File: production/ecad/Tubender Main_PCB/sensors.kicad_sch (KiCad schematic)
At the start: 6 parts, among them J10 640387-5, J14 640387-3, J5 640387-6, J6 640387-6, J8 640387-6, J9 640387-5

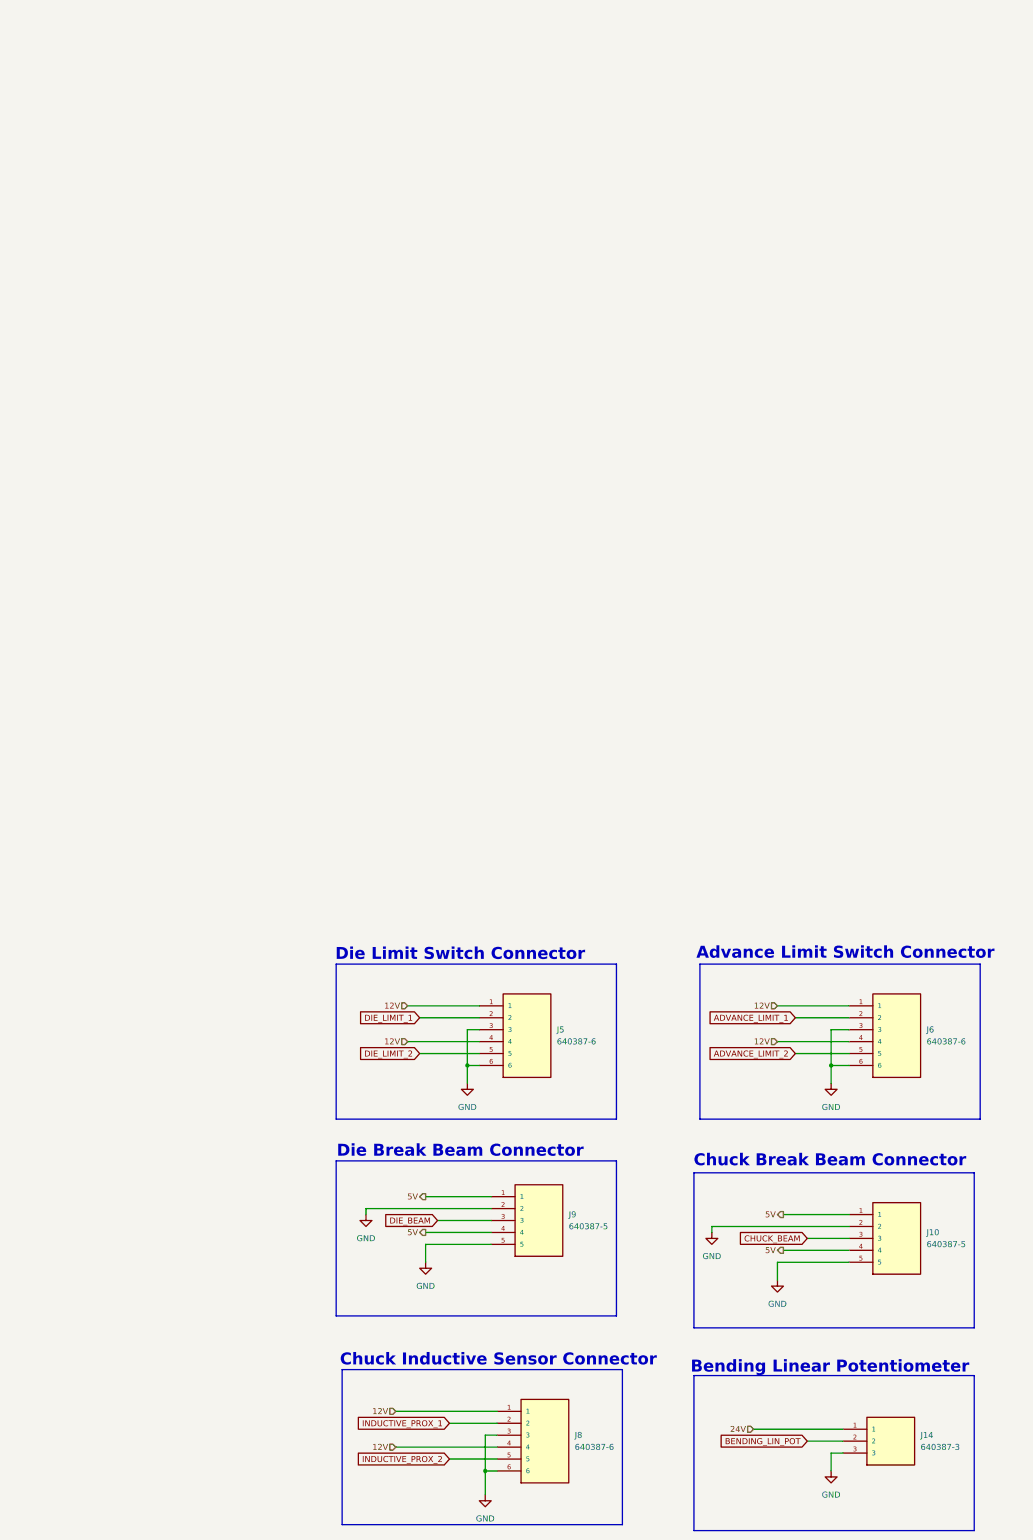
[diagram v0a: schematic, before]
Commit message: Fixed the Nets
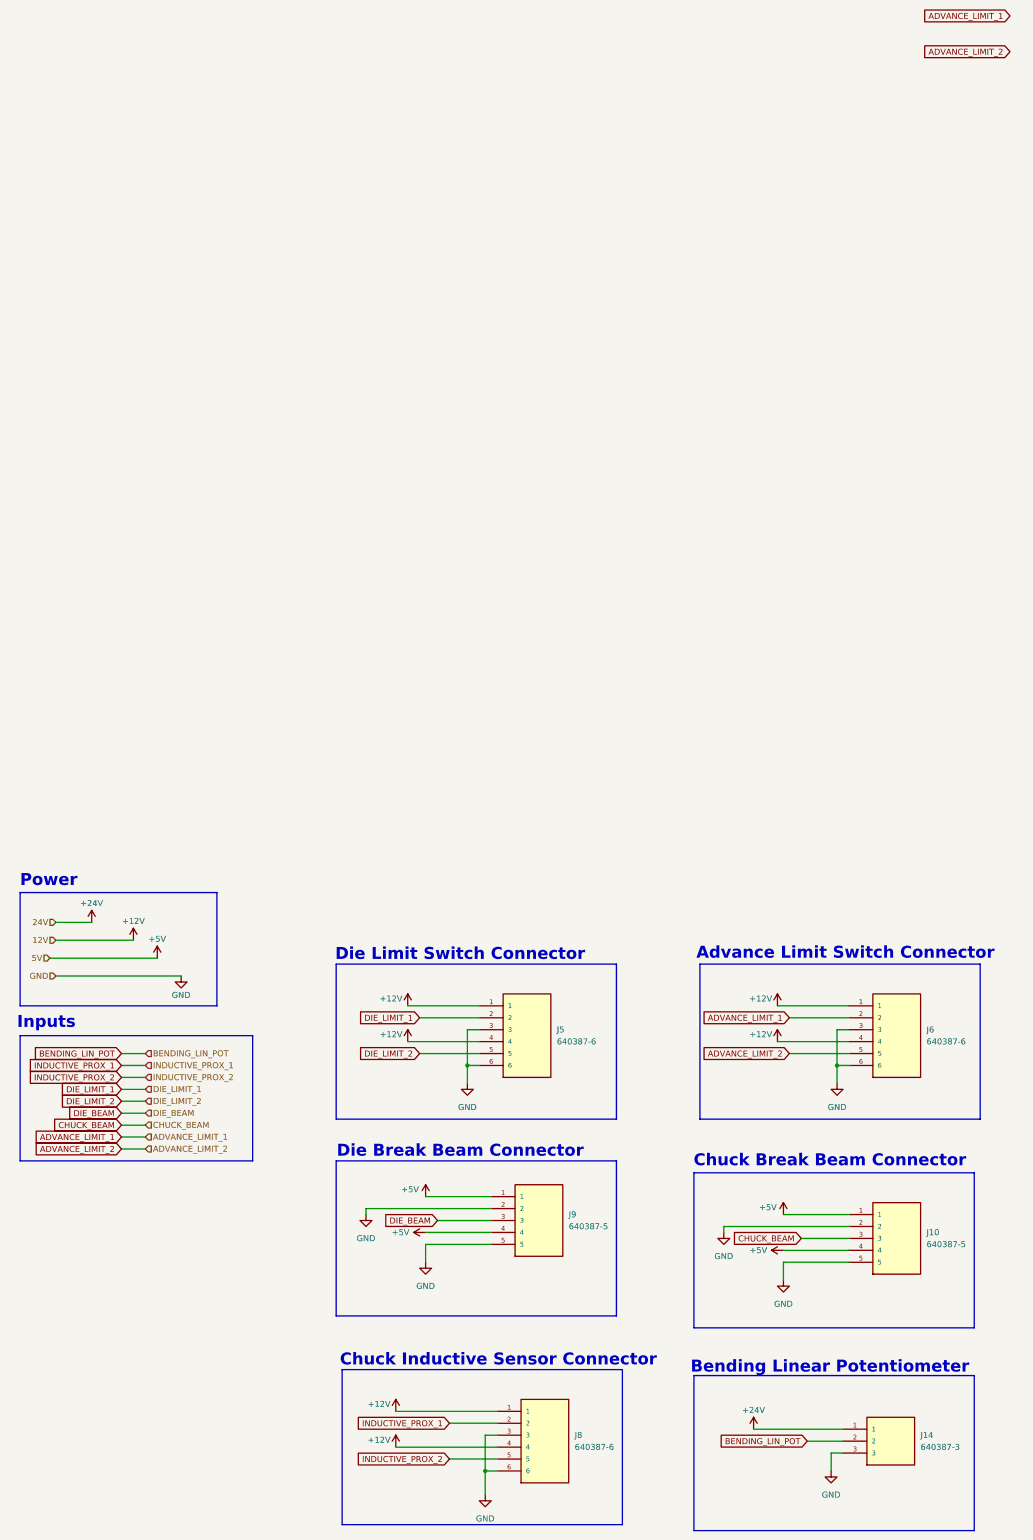
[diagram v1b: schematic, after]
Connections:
- net 12V renamed +12V
- net 24V renamed +24V
- net 5V renamed +5V
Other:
- note added: "Inputs"
- note added: "Power"
